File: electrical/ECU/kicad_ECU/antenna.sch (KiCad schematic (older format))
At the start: 4 parts

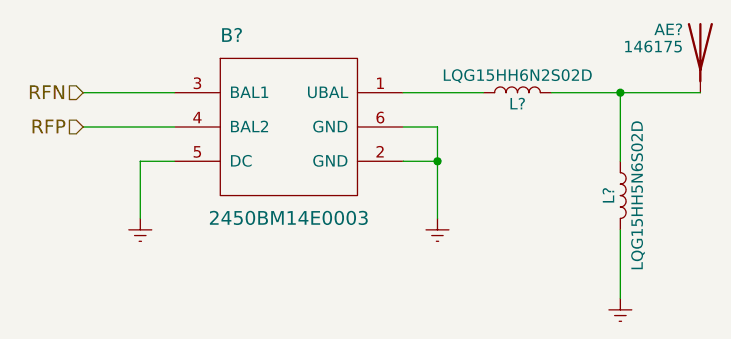
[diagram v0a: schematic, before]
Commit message: fixed some naming errors and initial round of double checking
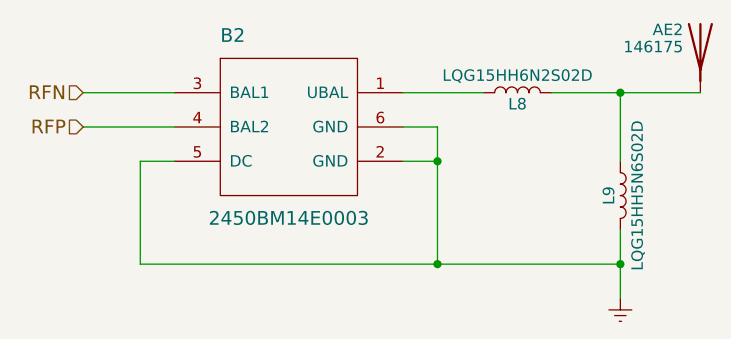
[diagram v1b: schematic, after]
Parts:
- gave numbers to parts that had none: 4
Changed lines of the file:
@@
 $Descr A4 11693 8268
 encoding utf-8
-Sheet 8 33
+Sheet 32 33
 Title "Antenna"
 Date ""
@@
 $EndDescr
 $Comp
-L 2450BM14E0003 B?
+L 2450BM14E0003 B1
 U 1 1 59818520
 P 5750 3350
-F 0 "B?" H 5450 3750 60  0000 L CNN
+AR Path="/597003E2/598181D1/59818520" Ref="B1"  Part="1"
+AR Path="/5978A36B/59800725/59818520" Ref="B2"  Part="1"
+F 0 "B2" H 5450 3750 60  0000 L CNN
 F 1 "2450BM14E0003" H 5750 2950 60  0000 C CNN
 F 2 "" H 5750 3350 60  0000 C CNN
@@
 $EndComp
 $Comp
-L Earth #PWR?
-U 1 1 59818529
-P 5100 3750
-F 0 "#PWR?" H 5100 3500 50  0001 C CNN
-F 1 "Earth" H 5100 3600 50  0001 C CNN
-F 2 "" H 5100 3750 50  0001 C CNN
-F 3 "" H 5100 3750 50  0001 C CNN
-	1    5100 3750
-	1    0    0    -1
-$EndComp
-$Comp
-L Earth #PWR?
-U 1 1 5981852F
-P 6400 3750
-F 0 "#PWR?" H 6400 3500 50  0001 C CNN
-F 1 "Earth" H 6400 3600 50  0001 C CNN
-F 2 "" H 6400 3750 50  0001 C CNN
-F 3 "" H 6400 3750 50  0001 C CNN
-	1    6400 3750
-	1    0    0    -1
-$EndComp
-$Comp
-L L L?
+L L L5
 U 1 1 59818535
 P 6750 3200
-F 0 "L?" V 6700 3200 50  0000 C CNN
+AR Path="/597003E2/598181D1/59818535" Ref="L5"  Part="1"
+AR Path="/5978A36B/59800725/59818535" Ref="L8"  Part="1"
+F 0 "L8" V 6700 3200 50  0000 C CNN
 F 1 "LQG15HH6N2S02D" V 6825 3200 50  0000 C CNN
 F 2 "" H 6750 3200 50  0001 C CNN
@@
 $EndComp
 $Comp
-L Antenna AE?
+L Antenna AE1
 U 1 1 5981853C
 P 7550 3000
-F 0 "AE?" H 7475 3075 50  0000 R CNN
+AR Path="/597003E2/598181D1/5981853C" Ref="AE1"  Part="1"
+AR Path="/5978A36B/59800725/5981853C" Ref="AE2"  Part="1"
+F 0 "AE2" H 7475 3075 50  0000 R CNN
 F 1 "146175" H 7475 3000 50  0000 R CNN
 F 2 "" H 7550 3000 50  0001 C CNN
@@
 $EndComp
 $Comp
-L L L?
+L L L6
 U 1 1 59818543
 P 7200 3650
-F 0 "L?" V 7150 3650 50  0000 C CNN
+AR Path="/597003E2/598181D1/59818543" Ref="L6"  Part="1"
+AR Path="/5978A36B/59800725/59818543" Ref="L9"  Part="1"
+F 0 "L9" V 7150 3650 50  0000 C CNN
 F 1 "LQG15HH5N6S02D" V 7275 3650 50  0000 C CNN
 F 2 "" H 7200 3650 50  0001 C CNN
@@
 $EndComp
 $Comp
-L Earth #PWR?
+L Earth #PWR26
 U 1 1 5981854A
 P 7200 4100
-F 0 "#PWR?" H 7200 3850 50  0001 C CNN
+AR Path="/597003E2/598181D1/5981854A" Ref="#PWR26"  Part="1"
+AR Path="/5978A36B/59800725/5981854A" Ref="#PWR69"  Part="1"
+F 0 "#PWR69" H 7200 3850 50  0001 C CNN
 F 1 "Earth" H 7200 3950 50  0001 C CNN
 F 2 "" H 7200 4100 50  0001 C CNN
@@
 	5250 3500 5100 3500
 Wire Wire Line
-	5100 3500 5100 3750
+	5100 3500 5100 3950
 Wire Wire Line
 	6250 3500 6400 3500
 Wire Wire Line
-	6400 3350 6400 3750
+	6400 3350 6400 3950
 Wire Wire Line
 	6250 3350 6400 3350
@@
 Text HLabel 4850 3350 0    60   Input ~ 0
 RFP
+Wire Wire Line
+	5100 3950 7200 3950
+Connection ~ 7200 3950
+Connection ~ 6400 3950
 $EndSCHEMATC
